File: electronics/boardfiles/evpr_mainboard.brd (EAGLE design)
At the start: 93.2 x 42.7 mm, 115 parts

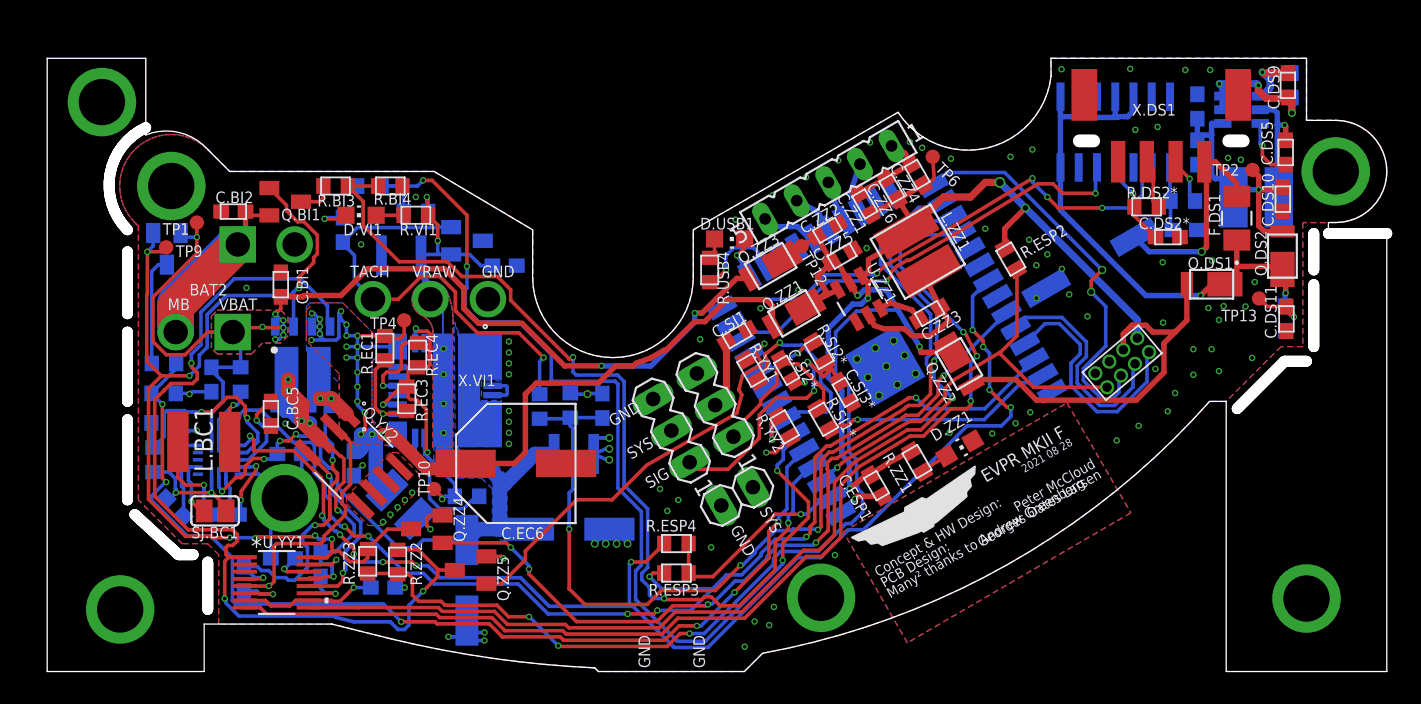
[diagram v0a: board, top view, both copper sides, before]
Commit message: Add hall-effect tachometer, remove old tach, large-scale silkscreen updates, minor updates to various components, removed strange void in internal layers
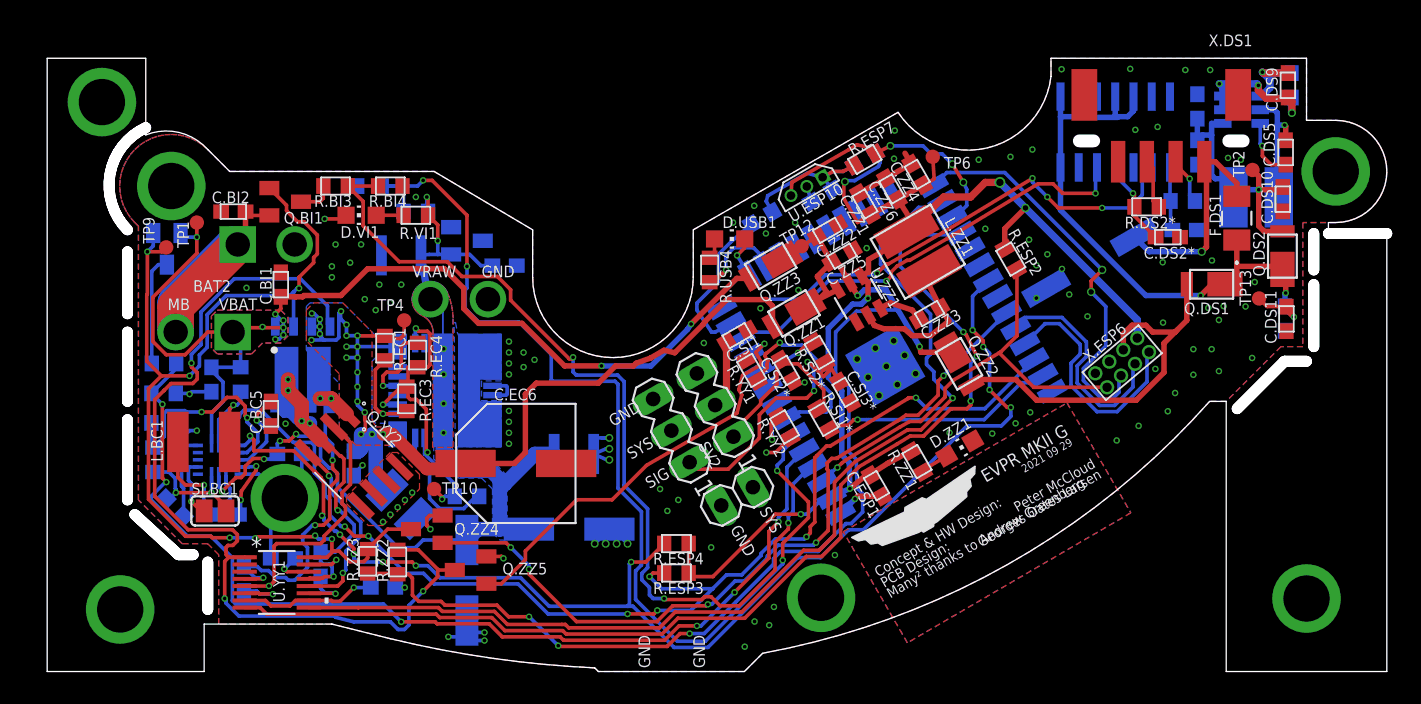
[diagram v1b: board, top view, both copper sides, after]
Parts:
- removed C.VI1, C.VI2*: 0.1uF, mccloud:C0603
- removed R.VI4: 100k, mccloud:R0603
- removed R.VI5: 22.1k, mccloud:R0603
- removed X.ESP1: (no value), con-lsta:FE05-1
- added C.ESP5: 0.1uF, mccloud:C0603
- added R.ESP7: 100k, mccloud:R0603
- added R.ESP8*, R.ESP9*: 0, mccloud:R0603
- added U.ESP10: HALLEFFECT, mccloud:1.27MMHALLEFECT
- X.VI1: value B3P-VH(LF)(SN) -> 2-THROUGHOLE-OFFSET; device mccloud:B3P-VH(LF)(SN) -> mccloud:2-THROUGH-HOLE-LARGE-OFFSET
- turned X.VI1 to 0 degrees
- renumbered SV1 to X.ESP6
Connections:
- removed net N$49: U.ESP1.19, X.ESP1.5
- removed net N$66: U.ESP1.20, X.ESP1.4
- removed net N$68: U.ESP1.21, X.ESP1.3
- removed net N$70: U.ESP1.22, X.ESP1.2
- removed net TACH: C.VI2*.1, R.VI4.1, R.VI5.2, U.ESP1.27
- removed net TACH_RAW: C.VI1.1, Q.VI1.2, R.VI4.2, X.VI1.3
- new net HALL: R.ESP7.2, U.ESP1.27, U.ESP10.P$3
- new net HALL_EN: R.ESP9*.2, U.ESP1.13
- new net N$1: C.ESP5.2, R.ESP7.1, R.ESP8*.1, R.ESP9*.1, U.ESP10.P$1
- net ESP_POWER: now also R.ESP8*.2
- net GND: now also C.ESP5.1, U.ESP10.P$2; no longer C.VI1.2, C.VI2*.2, R.VI5.1, X.ESP1.1
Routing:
- net TACH: track 67.4 -> 0.00 mm, vias 4 -> 0
- net TACH_RAW: track 31.5 -> 0.00 mm, vias 1 -> 0
- net HALL: track 0.00 -> 18.1 mm, vias 0 -> 3
- net N$1: track 0.00 -> 11.5 mm
- net HALL_EN: track 0.00 -> 10.9 mm
- net ESP_POWER: track 77.8 -> 85.7 mm, vias 5 -> 6
- net N$49: track 3.89 -> 0.00 mm
- net N$70: track 3.58 -> 0.00 mm
- net GND: track 72.7 -> 69.3 mm, vias 112 -> 122
- net N$66: track 3.11 -> 0.00 mm
- net N$68: track 2.90 -> 0.00 mm
- removed copper zone on layer 15, net AGND
- removed copper zone on layer 2, net AGND
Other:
- board text added: "2021 09 29"
- board text added: "EVPR MKII G"
- board text removed: "2021 08 28"
- board text removed: "EVPR MKII F"
- board text removed: "TACH"

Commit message: Update snapoffs to conform with OSH park recommendations, increase servo diameter, misc DRC corrections
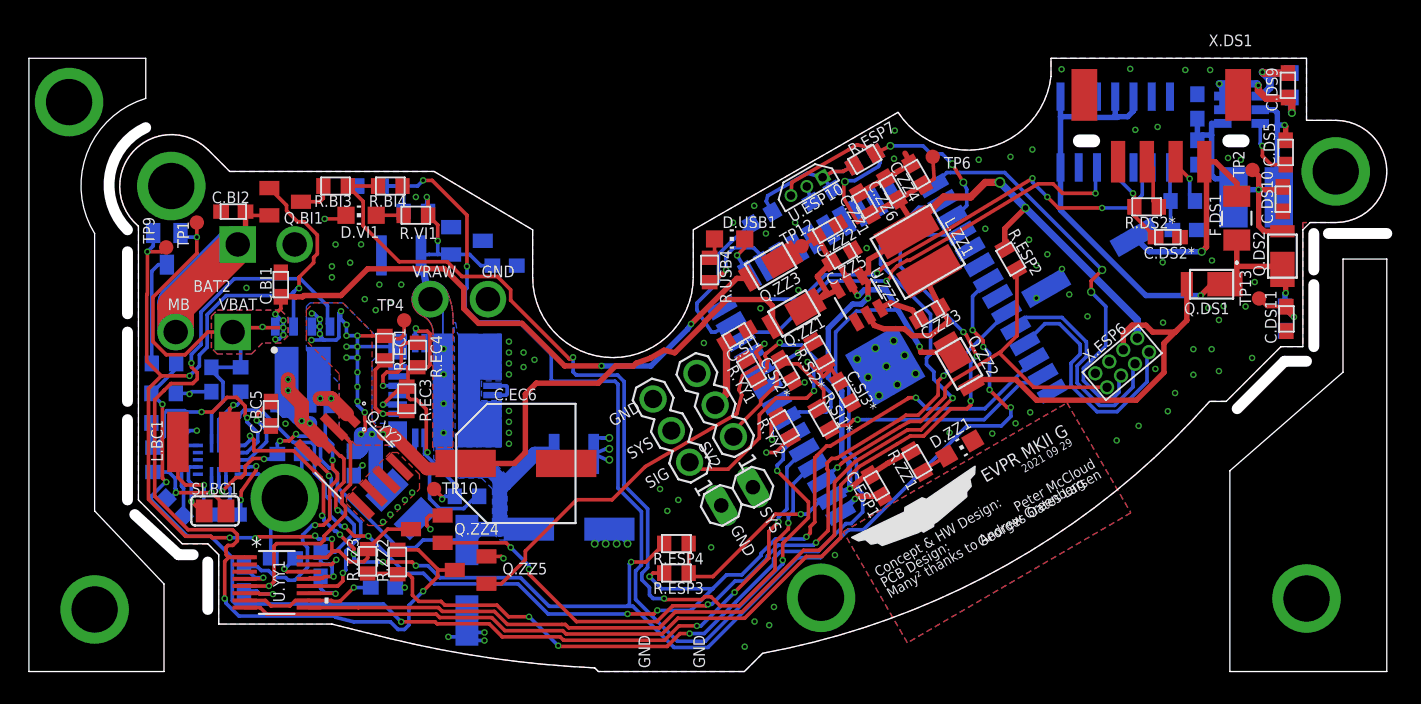
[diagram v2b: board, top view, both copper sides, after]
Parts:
- SV2, SV3: device con-lstb:MA03-1 -> mccloud:MA03-1
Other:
- board size 93.2 x 42.7 mm -> 94.5 x 42.7 mm

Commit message: Update snapoffs to conform with OSH park recommendations, increase servo diameter, misc DRC corrections
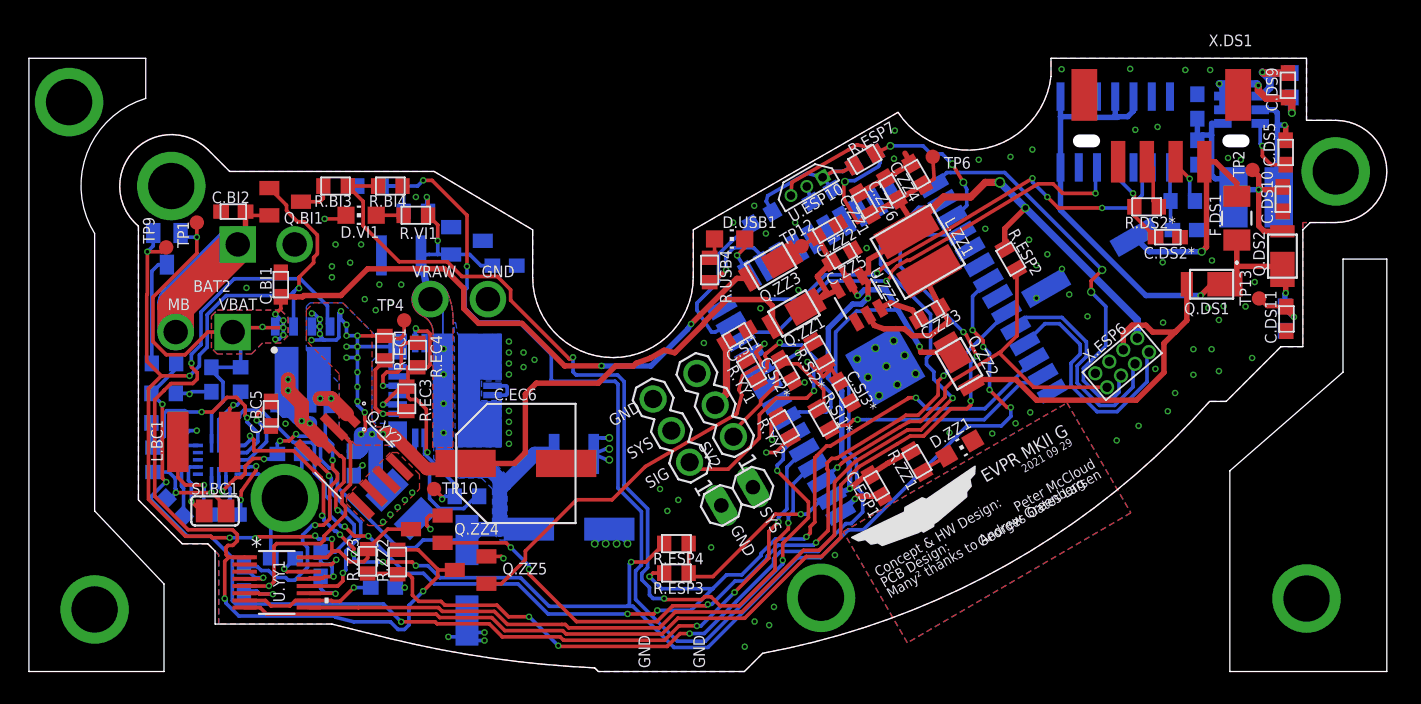
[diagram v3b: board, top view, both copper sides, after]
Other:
- outline, holes or cut-outs redrawn

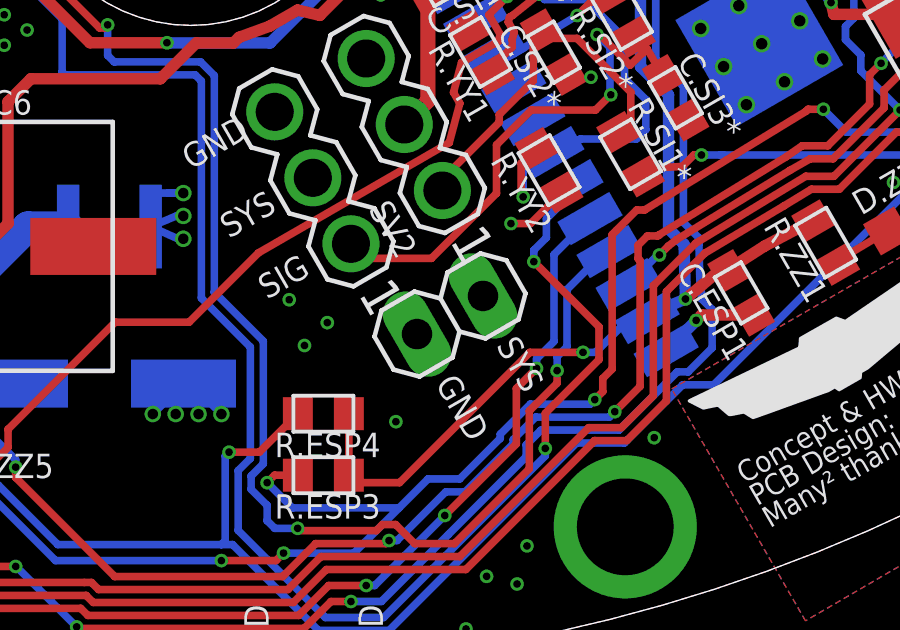
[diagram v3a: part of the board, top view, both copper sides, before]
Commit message: Incrase diameter on a couple of more holes
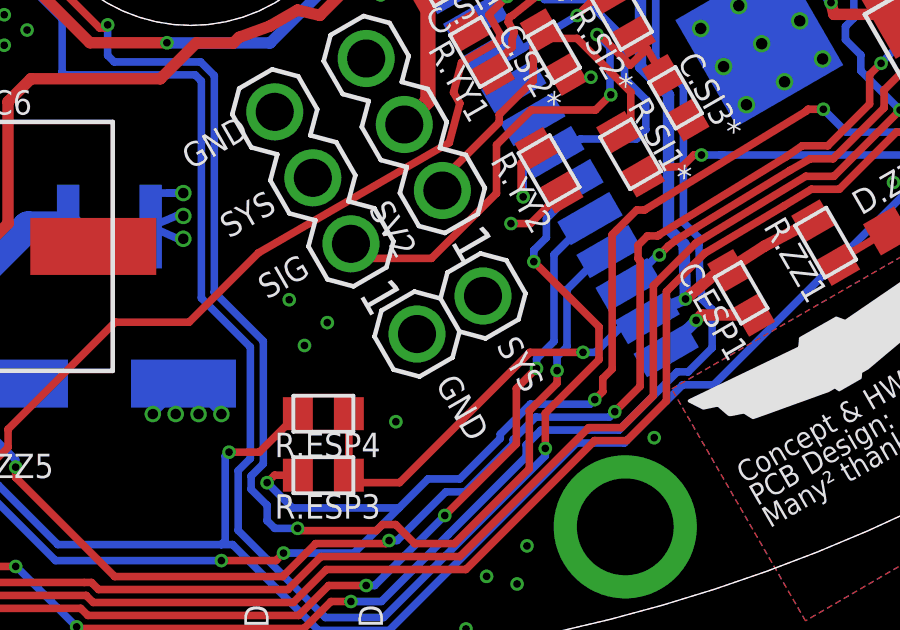
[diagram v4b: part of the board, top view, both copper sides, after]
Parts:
- JP1: device pinhead:1X02 -> mccloud:1X02
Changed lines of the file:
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@@
 <attribute name="VALUE" x="8.498659375" y="-41.20905625" size="1.27" layer="27" ratio="10" rot="R120"/>
 </element>
-<element name="JP1" library="pinhead" library_urn="urn:adsk.eagle:library:325" package="1X02" package3d_urn="urn:adsk.eagle:package:22435/2" value="" x="8.636" y="-43.942" smashed="yes" rot="R30">
+<element name="JP1" library="mccloud" package="1X02" package3d_urn="urn:adsk.eagle:package:22435/2" value="" x="8.636" y="-43.942" smashed="yes" rot="R30">
 <attribute name="POPULARITY" value="98" x="8.636" y="-43.942" size="1.778" layer="27" rot="R30" display="off"/>
 <attribute name="VALUE" x="8.02379375" y="-47.961628125" size="1.27" layer="27" rot="R30"/>

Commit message: Various finishing touches
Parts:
- removed JP1: (no value), mccloud:1X02
- removed R.ESP7: 100k, mccloud:R0603
- removed R.ESP8*: 0, mccloud:R0603
- added R.TK2: 0, mccloud:R0603
- added R.TK3: 100k, mccloud:R0603
- added SV1: (no value), mccloud:MA03-1
- SV3: device mccloud:MA03-1 -> mccloud:1X02
- moved SV3 6.47 mm to (8.64, -43.9), turned to 30 degrees
- renumbered C.ESP5 to C.TK1, R.ESP9* to R.TK1*, R.USB4 to R.ESP1, U.ESP10 to U.TK1
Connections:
- net ESP_POWER: now also R.TK2.2; no longer R.ESP8*.2
- net GND: now also SV1.3, SV3.1; no longer JP1.1, SV3.3
- net HALL: now also R.TK3.2; no longer R.ESP7.2
- net N$1: now also R.TK2.1, R.TK3.1; no longer R.ESP7.1, R.ESP8*.1
- net N$12: now also SV1.1; no longer SV3.1
- net SYS_POWER: now also SV1.2; no longer JP1.2
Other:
- board text added: "2022 01 05"
- board text added: "EVPR MKII H"
- board text added: "VB"
- board text removed: "2021 09 29"
- board text removed: "EVPR MKII G"
